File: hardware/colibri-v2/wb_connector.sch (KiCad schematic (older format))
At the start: 2 parts

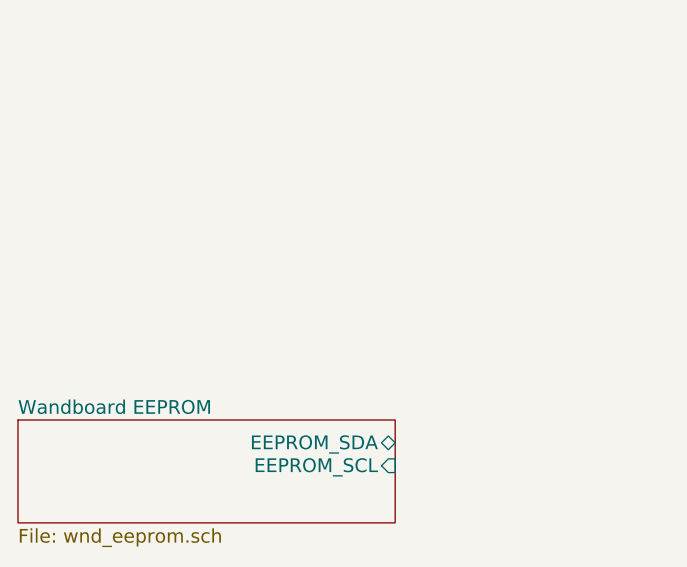
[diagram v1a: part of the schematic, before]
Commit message: Added connection between wandboard and cortex USB FS2
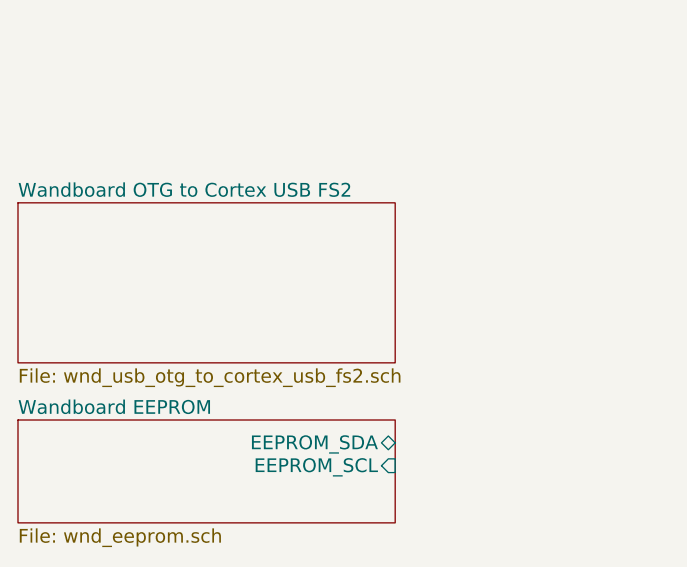
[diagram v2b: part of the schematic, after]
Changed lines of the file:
@@
 $Descr A3 16535 11693
 encoding utf-8
-Sheet 11 26
+Sheet 11 27
 Title ""
 Date ""
@@
 F3 "EEPROM_SCL" I R 2550 8350 60
 $EndSheet
+$Sheet
+S 900  7200 1650 700
+U 567A4150
+F0 "Wandboard OTG to Cortex USB FS2" 60
+F1 "wnd_usb_otg_to_cortex_usb_fs2.sch" 60
+$EndSheet
 $EndSCHEMATC

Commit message: work on wandboard service sheet.
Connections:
- net EIM_DA12: now reaches CN?.255
- net EIM_DA11: now reaches CN?.256
- net EIM_D27: now reaches CN?.258
- net EIM_D26: now reaches CN?.259
- net EIM_BCLK: now reaches CN?.260
- net EIM_DA8: now reaches CN?.261
- net ENET_RX_ER: now reaches CN?.262
- net GPIO_19: now reaches CN?.263
- net GPIO7_IO08: now reaches CN?.264
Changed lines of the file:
@@
 $Descr A3 16535 11693
 encoding utf-8
-Sheet 11 27
+Sheet 11 28
 Title ""
 Date ""
@@
 ???
 $Sheet
-S 900  8900 1650 550
+S 900  8200 1650 550
 U 565FC76D
 F0 "Wandboard RTC" 60
 F1 "wnd_rtc.sch" 60
-F2 "RTC_SDA" B R 2550 9000 60
-F3 "RTC_SCL" I R 2550 9100 60
-F4 "RTC_INT" O R 2550 9200 60
-$EndSheet
-$Sheet
-S 900  8150 1650 450
+F2 "RTC_SDA" B R 2550 8300 60
+F3 "RTC_SCL" I R 2550 8400 60
+F4 "RTC_INT" O R 2550 8500 60
+$EndSheet
+$Sheet
+S 900  7450 1650 450
 U 56693441
 F0 "Wandboard EEPROM" 60
 F1 "wnd_eeprom.sch" 60
-F2 "EEPROM_SDA" B R 2550 8250 60
-F3 "EEPROM_SCL" I R 2550 8350 60
-$EndSheet
-$Sheet
-S 900  7200 1650 700
+F2 "EEPROM_SDA" B R 2550 7550 60
+F3 "EEPROM_SCL" I R 2550 7650 60
+$EndSheet
+$Sheet
+S 900  6500 1650 700
 U 567A4150
 F0 "Wandboard OTG to Cortex USB FS2" 60
 F1 "wnd_usb_otg_to_cortex_usb_fs2.sch" 60
 $EndSheet
+$Sheet
+S 900  9100 1650 1900
+U 56AAE817
+F0 "Wandboard Service" 60
+F1 "wnd_service.sch" 60
+$EndSheet
+Text Label 8500 7500 0    60   ~ 0
+GPIO3_IO12
+Text Label 9100 7500 0    60   ~ 0
+EIM_DA12
+Text Label 9100 7800 0    60   ~ 0
+EIM_DA8
+Text Label 8500 7800 0    60   ~ 0
+GPIO3_IO08
+Text Label 8500 7900 0    60   ~ 0
+GPIO_19
+Wire Wire Line
+	8500 7700 9600 7700
+Wire Wire Line
+	8500 7800 9600 7800
+Wire Wire Line
+	8500 7900 9600 7900
+Text Label 8500 7700 0    60   ~ 0
+GPIO3_IO26
+Text Label 9100 7700 0    60   ~ 0
+EIM_D26
+Wire Wire Line
+	8500 7500 9600 7500
+Text Label 11600 7500 2    60   ~ 0
+EIM_DA11
+Text Label 12200 7500 2    60   ~ 0
+GPIO3_IO11
+Text Label 11600 7600 2    60   ~ 0
+EIM_D27
+Text Label 12200 7600 2    60   ~ 0
+GPIO3_IO27
+Text Label 11600 7700 2    60   ~ 0
+EIM_BCLK
+Text Label 12200 7700 2    60   ~ 0
+GPIO6_IO31
+Text Label 11600 7800 2    60   ~ 0
+ENET_RX_ER
+Text Label 12200 7800 2    60   ~ 0
+GPIO1_IO26
+Text Label 11600 7900 2    60   ~ 0
+SD3_RST
+Text Label 12200 7900 2    60   ~ 0
+GPIO7_IO08
+Wire Wire Line
+	11000 7500 12200 7500
+Wire Wire Line
+	11000 7600 12200 7600
+Wire Wire Line
+	11000 7700 12200 7700
+Wire Wire Line
+	11000 7800 12200 7800
+Wire Wire Line
+	11000 7900 12200 7900
 $EndSCHEMATC

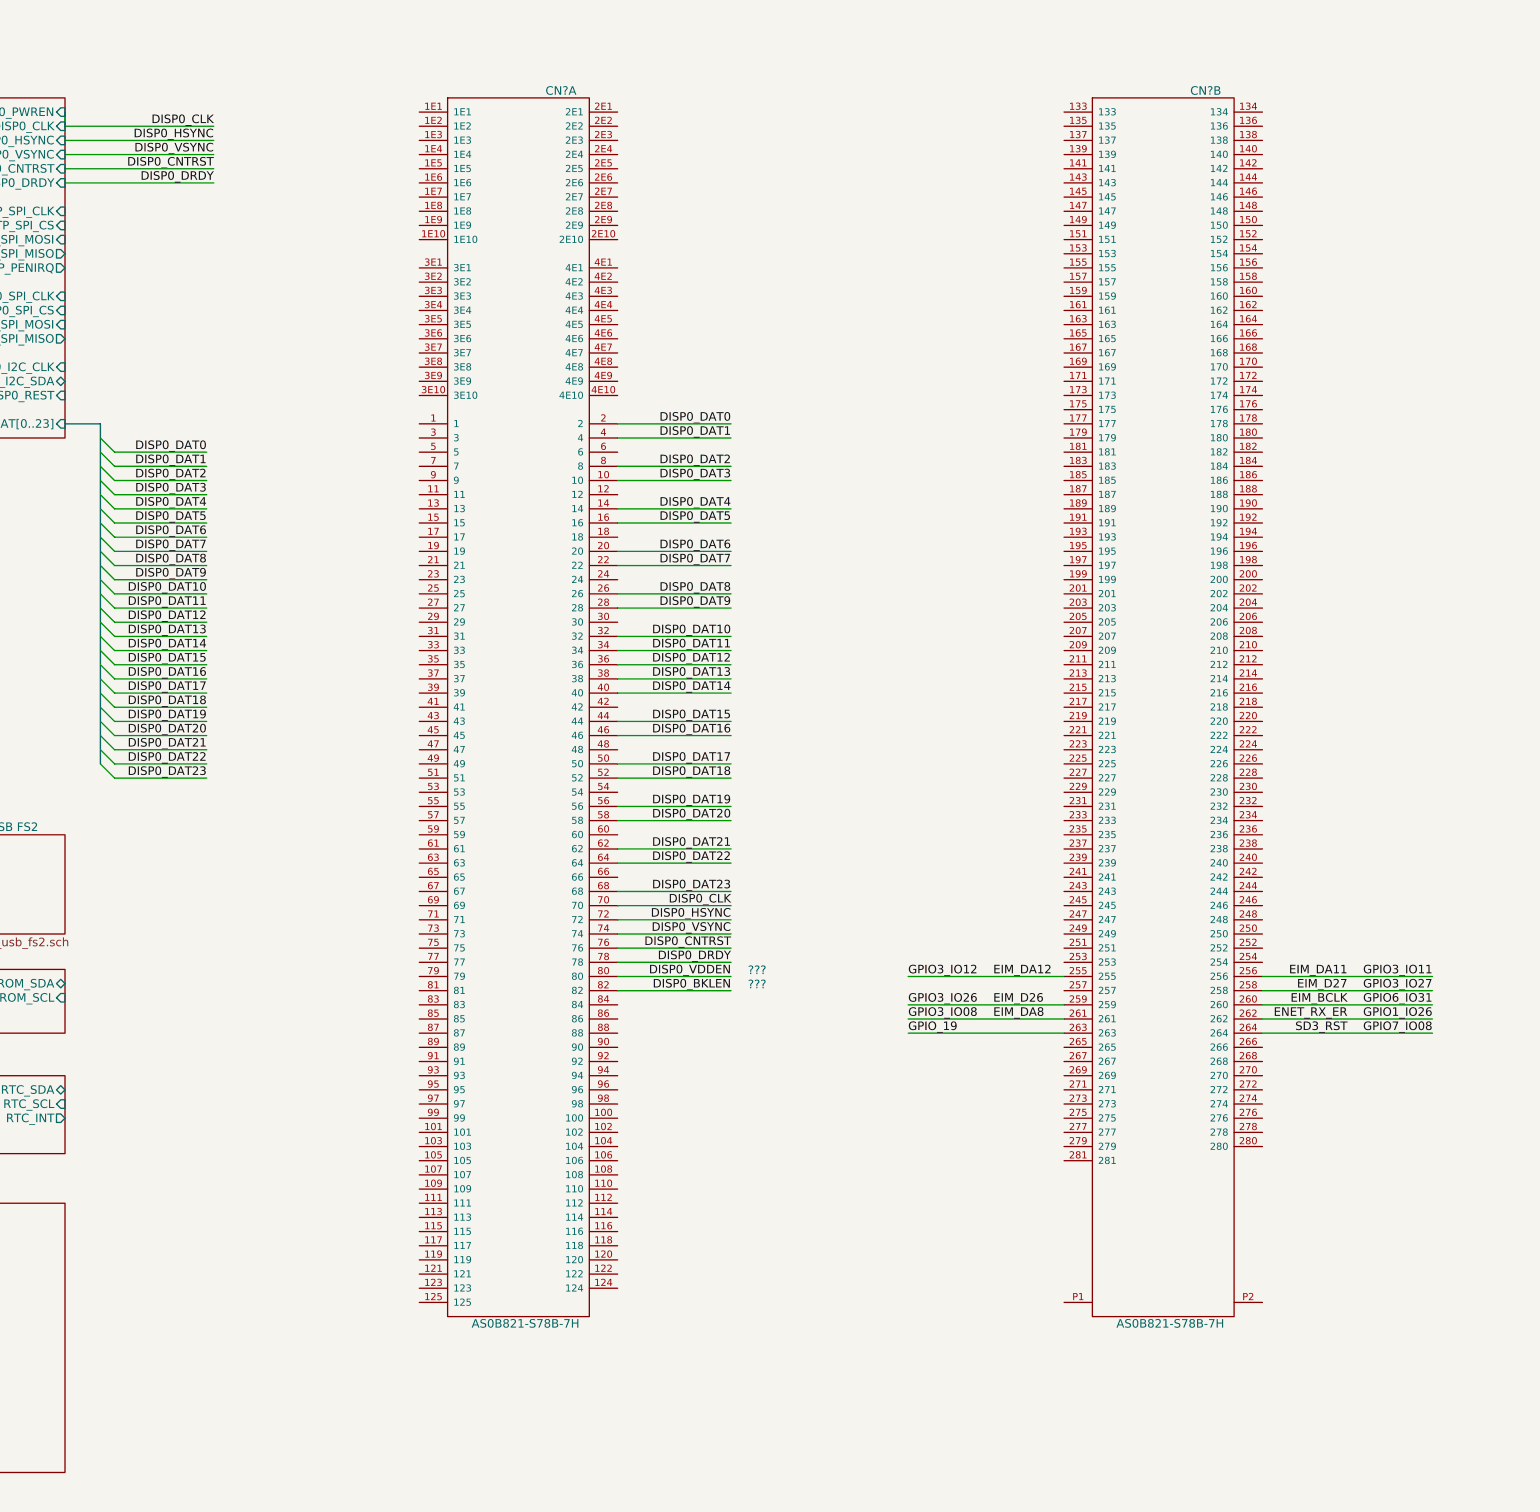
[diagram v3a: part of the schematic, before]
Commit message: Wired SDRAM pins. Added reset, power on/off for the WB module
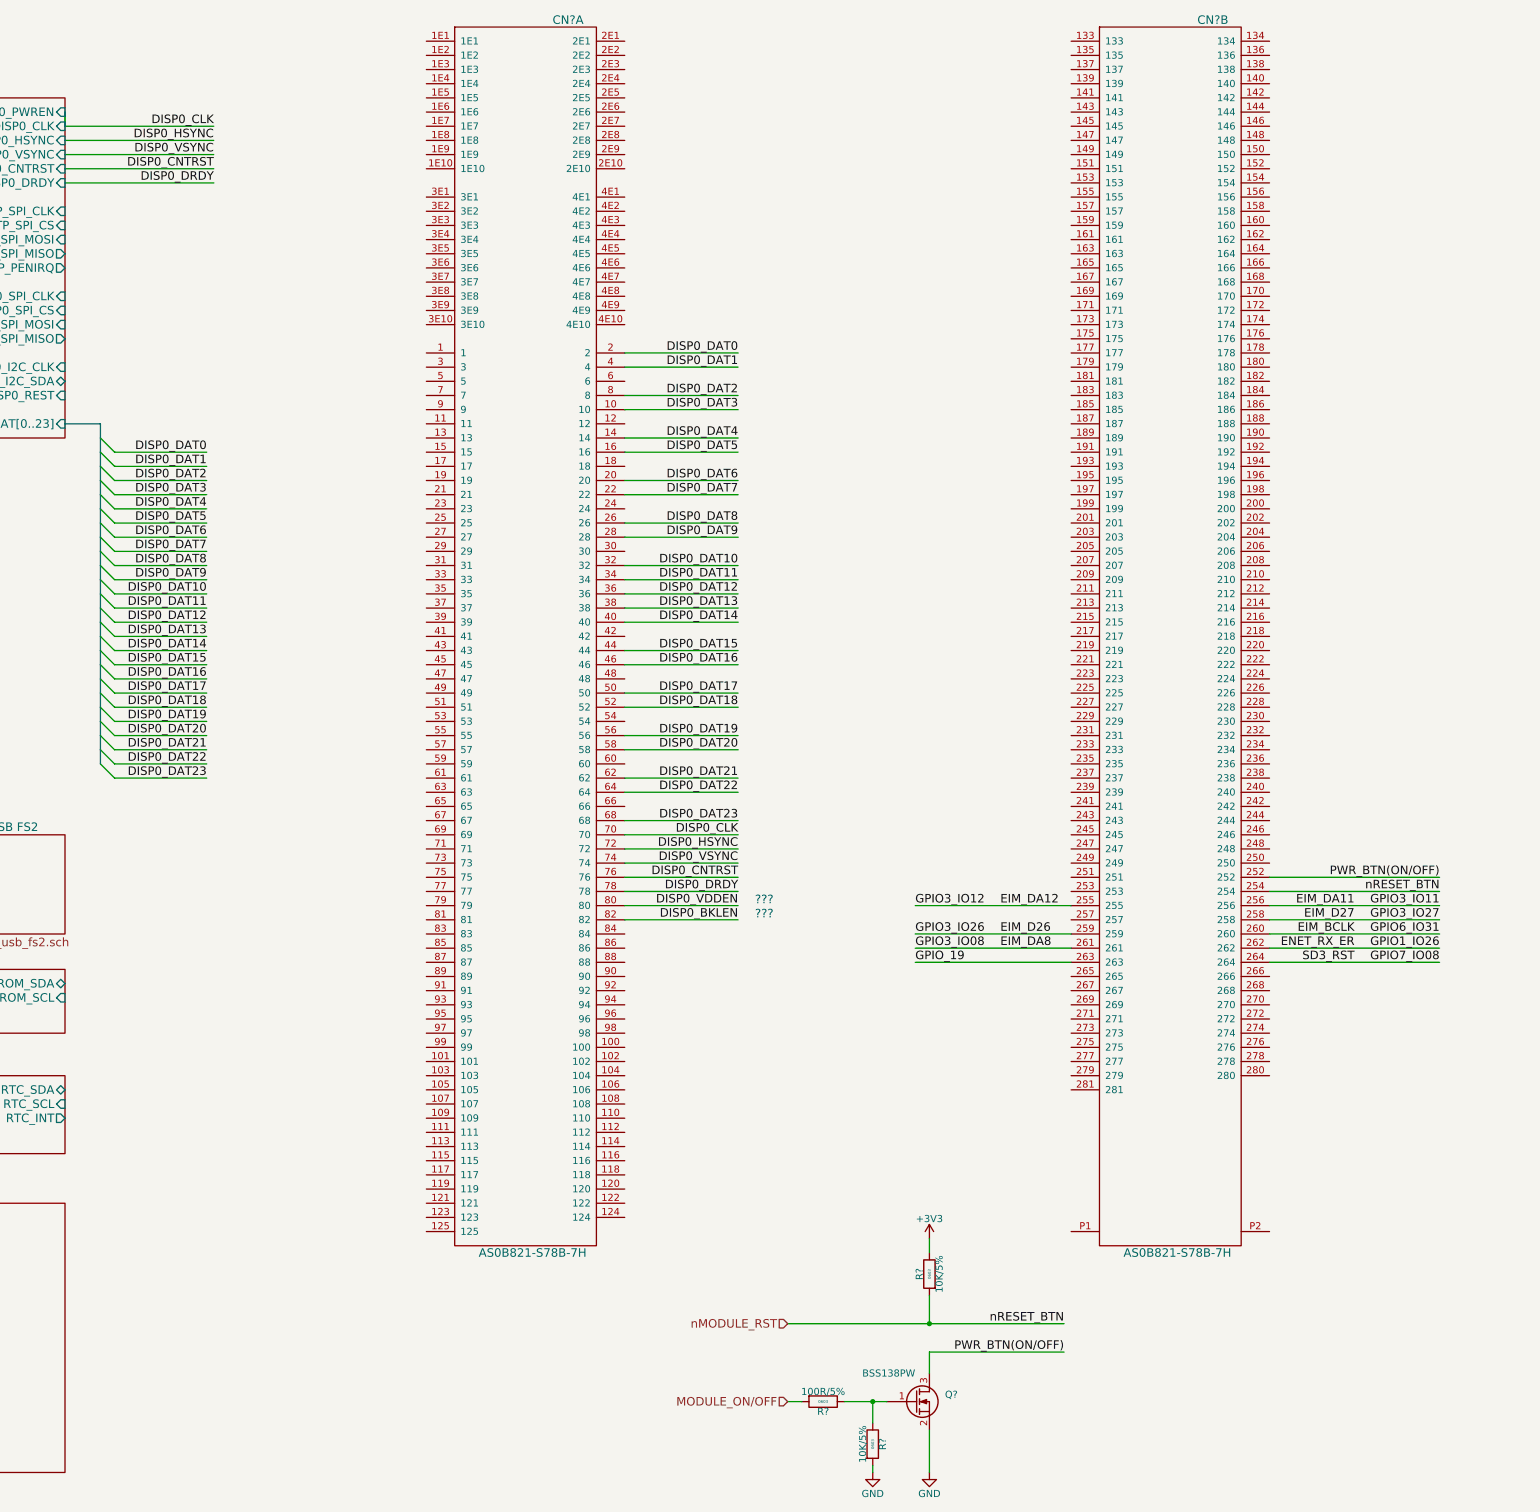
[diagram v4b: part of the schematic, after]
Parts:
- added Q?: BSS138PW, symbol Q_NMOS_GSD
- added R? (x2): 10K/5%, Resistors_SMD:R_0603, symbol R_SMT
- added R?: 100R/5%, Resistors_SMD:R_0603, symbol R_SMT
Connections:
- net PWR_BTN(ON/OFF): now reaches CN?.252
- net PWR_BTN(ON/OFF): now also Q?.3 (D)
- net nMODULE_RST: now reaches CN?.254
- net nMODULE_RST: now also R?.2
- new net: Q?.1 (G), R?.1, R?.1
- new net +3V3: R?.1
- new net GND: Q?.2 (S), R?.2
- new net MODULE_ON/OFF: R?.2
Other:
- moved on the sheet: CN?A, CN?B

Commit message: work on sheets wiring
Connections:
- net nMODULE_RST renamed MODULE_RSTn
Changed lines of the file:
@@
 $Descr A3 16535 11693
 encoding utf-8
-Sheet 11 28
+Sheet 10 28
 Title ""
 Date ""
@@
 	2550 3600 2800 3600
 Wire Bus Line
-	2800 3600 2800 3700
-Wire Bus Line
-	2800 3700 2800 3800
-Wire Bus Line
-	2800 3800 2800 3900
-Wire Bus Line
-	2800 3900 2800 4000
-Wire Bus Line
-	2800 4000 2800 4100
-Wire Bus Line
-	2800 4100 2800 4200
-Wire Bus Line
-	2800 4200 2800 4300
-Wire Bus Line
-	2800 4300 2800 4400
-Wire Bus Line
-	2800 4400 2800 4500
-Wire Bus Line
-	2800 4500 2800 4600
-Wire Bus Line
-	2800 4600 2800 4700
-Wire Bus Line
-	2800 4700 2800 4800
-Wire Bus Line
-	2800 4800 2800 4900
-Wire Bus Line
-	2800 4900 2800 5000
-Wire Bus Line
-	2800 5000 2800 5100
-Wire Bus Line
-	2800 5100 2800 5200
-Wire Bus Line
-	2800 5200 2800 5300
-Wire Bus Line
-	2800 5300 2800 5400
-Wire Bus Line
-	2800 5400 2800 5500
-Wire Bus Line
-	2800 5500 2800 5600
-Wire Bus Line
-	2800 5600 2800 5700
-Wire Bus Line
-	2800 5700 2800 5800
-Wire Bus Line
-	2800 5800 2800 5900
-Wire Bus Line
-	2800 5900 2800 6000
+	2800 3600 2800 6000
 Entry Wire Line
 	2800 3700 2900 3800
@@
 	11050 7400 12250 7400
 Text Label 12250 6900 2    60   ~ 0
-nRESET_BTN
+RESET_BTNn
 Text Label 12250 6800 2    60   ~ 0
 PWR_BTN(ON/OFF)
@@
 Wire Wire Line
 	11050 6800 12250 6800
-Text Label 9600 9950 2    60   ~ 0
-nRESET_BTN
 Text Label 9600 10150 2    60   ~ 0
 PWR_BTN(ON/OFF)
@@
 	8650 10150 9600 10150
 Text HLabel 7650 9950 0    60   Input ~ 0
-nMODULE_RST
-Wire Wire Line
-	9600 9950 8650 9950
-Wire Wire Line
-	8650 9950 7650 9950
+MODULE_RSTn
+Wire Wire Line
+	7650 9950 9600 9950
 $Comp
 L +3V3 #PWR?
@@
 	8250 10950 8250 11000
 Wire Wire Line
-	8050 10500 8250 10500
-Wire Wire Line
-	8250 10500 8350 10500
+	8050 10500 8350 10500
 Wire Wire Line
 	8250 10500 8250 10650
@@
 Wire Wire Line
 	8650 10150 8650 10300
+Text Label 9600 9950 2    60   ~ 0
+RESET_BTNn
 $EndSCHEMATC

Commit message: work on sheets wiring
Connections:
- net WB_UART_CTS: now reaches CN?.234
- net WB_UART_TX: now reaches CN?.236
- net WB_UART_RX: now reaches CN?.238
- net WB_UART_RTS: now reaches CN?.240
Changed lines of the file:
@@
 Text Label 9600 9950 2    60   ~ 0
 RESET_BTNn
+Text HLabel 11600 5900 2    60   Output ~ 0
+WB_UART_CTS
+Text HLabel 11600 6200 2    60   Input ~ 0
+WB_UART_RTS
+Text HLabel 11600 6000 2    60   Output ~ 0
+WB_UART_TX
+Text HLabel 11600 6100 2    60   Input ~ 0
+WB_UART_RX
+Wire Wire Line
+	11050 5900 11600 5900
+Wire Wire Line
+	11050 6000 11600 6000
+Wire Wire Line
+	11050 6100 11600 6100
+Wire Wire Line
+	11050 6200 11600 6200
 $EndSCHEMATC
